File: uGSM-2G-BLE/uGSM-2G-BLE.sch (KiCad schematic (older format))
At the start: 0 parts

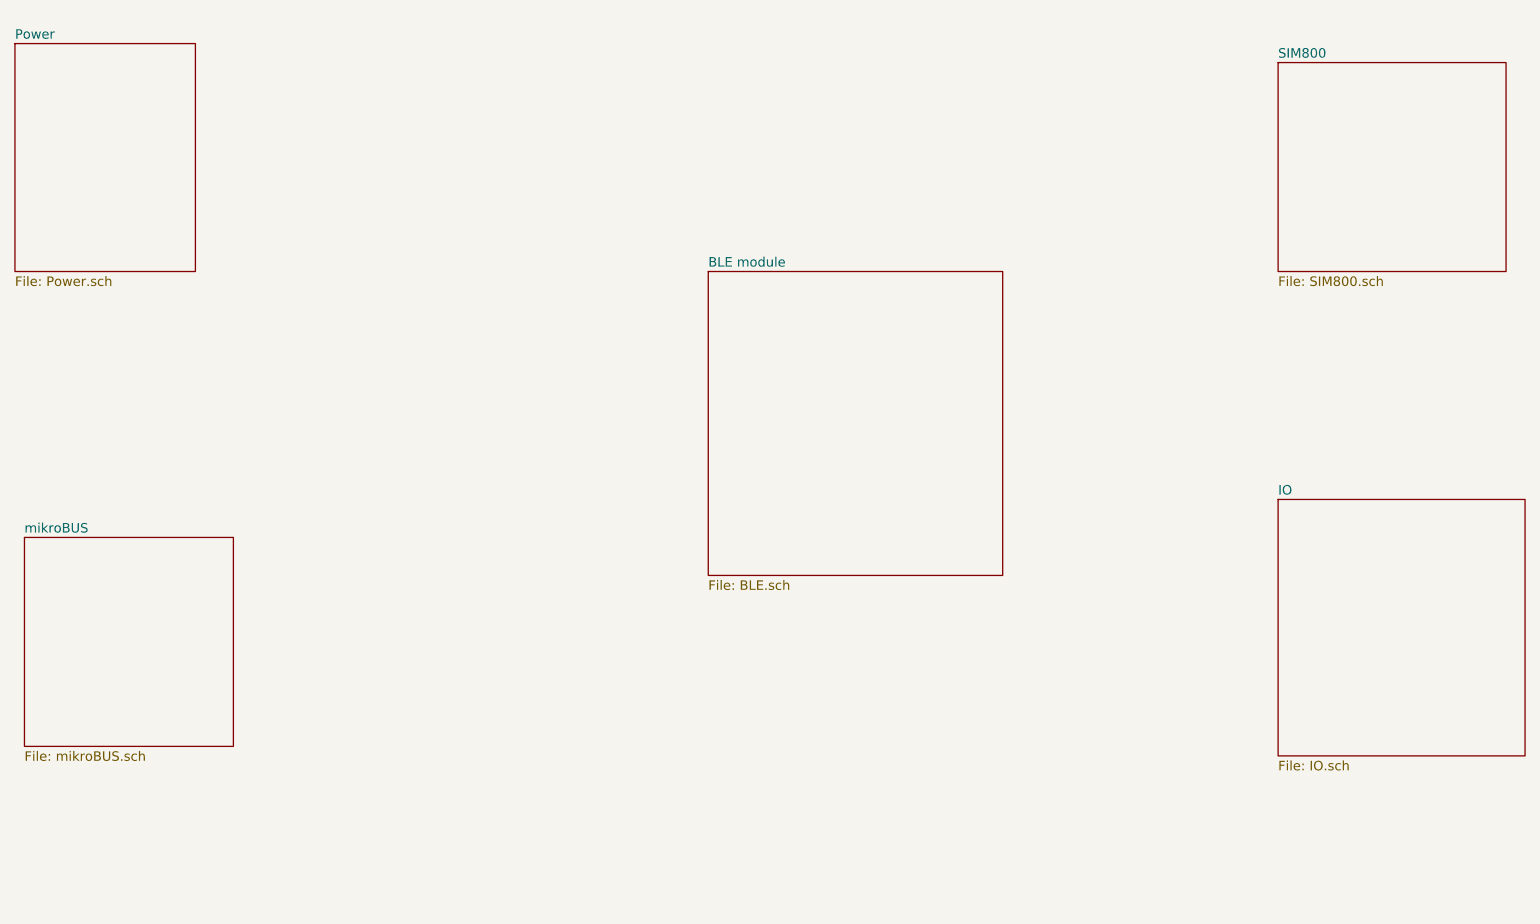
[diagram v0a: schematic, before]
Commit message: added sim800c stuff - needs checking
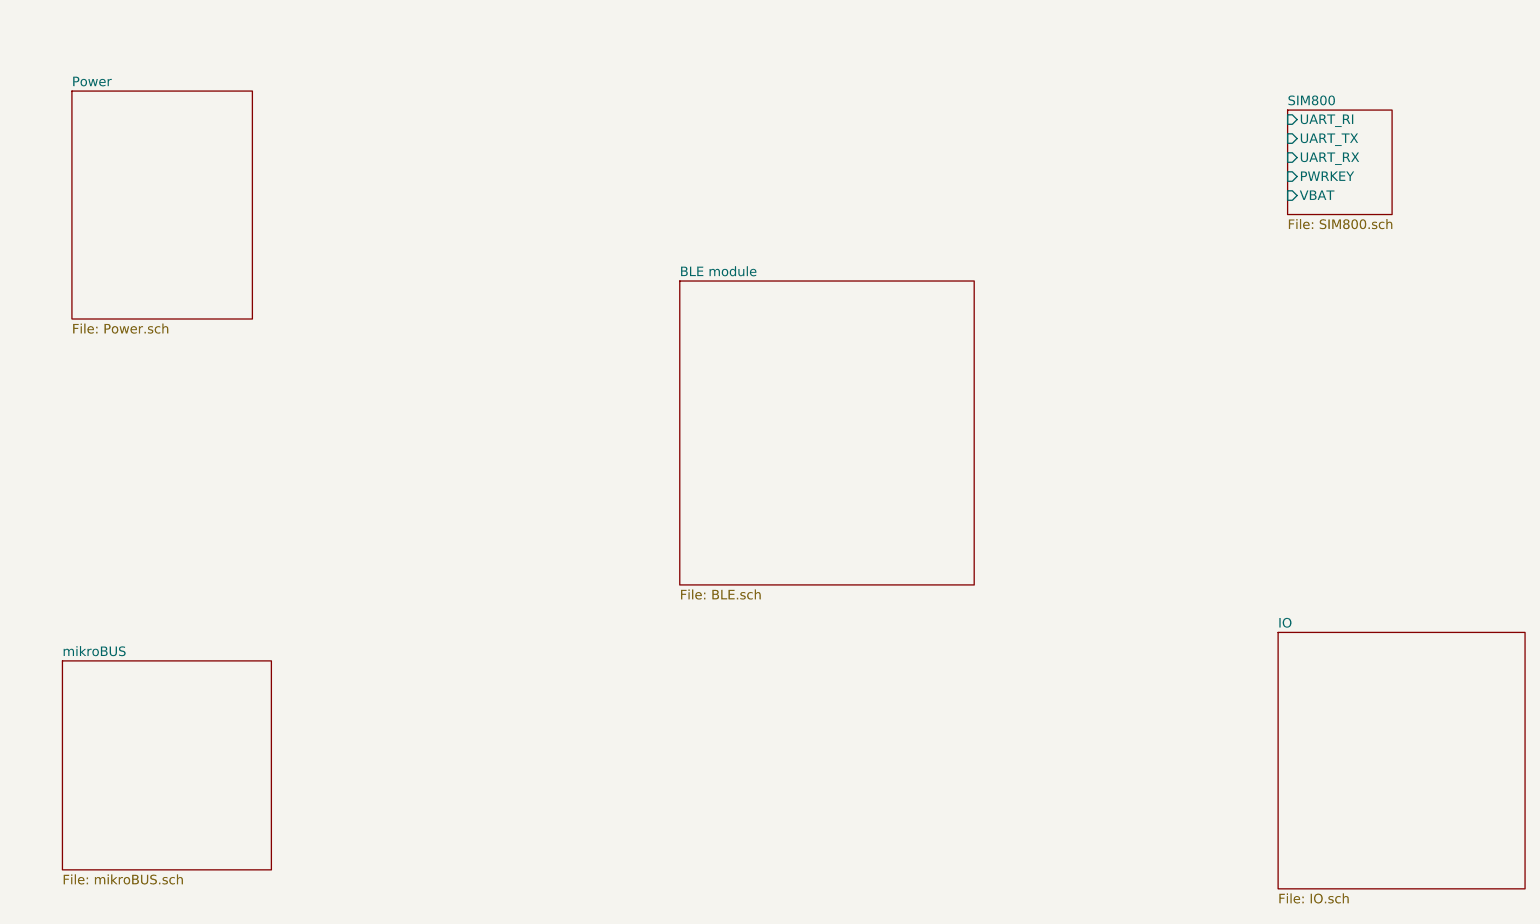
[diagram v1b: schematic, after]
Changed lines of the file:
@@
 $EndDescr
 $Sheet
-S 5350 2950 1550 1600
+S 5200 3000 1550 1600
 U 5E3D7DDA
 F0 "BLE module" 50
@@
 $EndSheet
 $Sheet
-S 1700 1750 950  1200
+S 2000 2000 950  1200
 U 5E3D7E07
 F0 "Power" 50
@@
 $EndSheet
 $Sheet
-S 1750 4350 1100 1100
+S 1950 5000 1100 1100
 U 5E3D7E1D
 F0 "mikroBUS" 50
@@
 $EndSheet
 $Sheet
-S 8350 1850 1200 1100
+S 8400 2100 550  550
 U 5E3D7E36
 F0 "SIM800" 50
 F1 "SIM800.sch" 50
+F2 "UART_TX" I L 8400 2250 50
+F3 "UART_RX" I L 8400 2350 50
+F4 "PWRKEY" I L 8400 2450 50
+F5 "VBAT" I L 8400 2550 50
+F6 "UART_RI" I L 8400 2150 50
 $EndSheet
 $Sheet
-S 8350 4150 1300 1350
+S 8350 4850 1300 1350
 U 5E3D7E53
 F0 "IO" 50

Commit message: ble connected to mikrobus
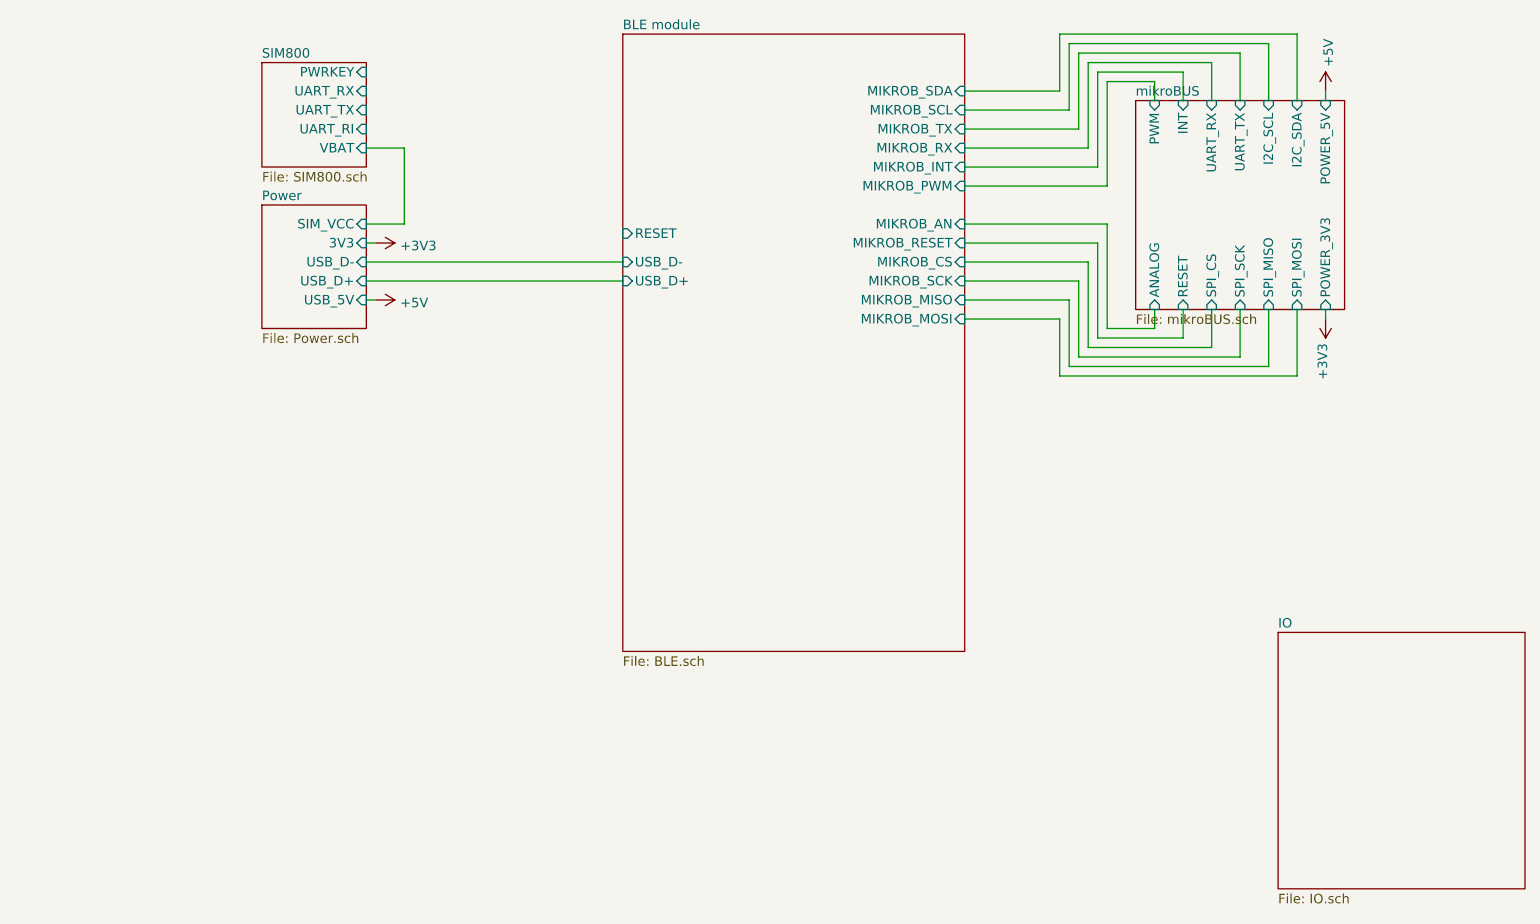
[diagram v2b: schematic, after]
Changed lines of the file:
@@
 $EndDescr
 $Sheet
-S 5200 3000 1550 1600
-U 5E3D7DDA
-F0 "BLE module" 50
-F1 "BLE.sch" 50
-$EndSheet
-$Sheet
-S 2000 2000 950  1200
+S 3000 2600 550  650
 U 5E3D7E07
 F0 "Power" 50
 F1 "Power.sch" 50
-$EndSheet
-$Sheet
-S 1950 5000 1100 1100
+F2 "SIM_VCC" I R 3550 2700 50
+F3 "3V3" I R 3550 2800 50
+F4 "USB_D-" I R 3550 2900 50
+F5 "USB_D+" I R 3550 3000 50
+F6 "USB_5V" I R 3550 3100 50
+$EndSheet
+$Sheet
+S 7600 2050 1100 1100
 U 5E3D7E1D
 F0 "mikroBUS" 50
 F1 "mikroBUS.sch" 50
-$EndSheet
-$Sheet
-S 8400 2100 550  550
+F2 "ANALOG" I B 7700 3150 50
+F3 "RESET" I B 7850 3150 50
+F4 "SPI_CS" I B 8000 3150 50
+F5 "SPI_SCK" I B 8150 3150 50
+F6 "SPI_MISO" I B 8300 3150 50
+F7 "SPI_MOSI" I B 8450 3150 50
+F8 "POWER_3V3" I B 8600 3150 50
+F9 "POWER_5V" I T 8600 2050 50
+F10 "I2C_SDA" I T 8450 2050 50
+F11 "I2C_SCL" I T 8300 2050 50
+F12 "UART_TX" I T 8150 2050 50
+F13 "UART_RX" I T 8000 2050 50
+F14 "INT" I T 7850 2050 50
+F15 "PWM" I T 7700 2050 50
+$EndSheet
+$Sheet
+S 3000 1850 550  550
 U 5E3D7E36
 F0 "SIM800" 50
 F1 "SIM800.sch" 50
-F2 "UART_TX" I L 8400 2250 50
-F3 "UART_RX" I L 8400 2350 50
-F4 "PWRKEY" I L 8400 2450 50
-F5 "VBAT" I L 8400 2550 50
-F6 "UART_RI" I L 8400 2150 50
+F2 "UART_TX" I R 3550 2100 50
+F3 "UART_RX" I R 3550 2000 50
+F4 "PWRKEY" I R 3550 1900 50
+F5 "VBAT" I R 3550 2300 50
+F6 "UART_RI" I R 3550 2200 50
 $EndSheet
 $Sheet
@@
 F1 "IO.sch" 50
 $EndSheet
+$Comp
+L power:+3V3 #PWR?
+U 1 1 5E4C2654
+P 3600 2800
+F 0 "#PWR?" H 3600 2650 50  0001 C CNN
+F 1 "+3V3" V 3615 2928 50  0000 L CNN
+F 2 "" H 3600 2800 50  0001 C CNN
+F 3 "" H 3600 2800 50  0001 C CNN
+	1    3600 2800
+	0    1    1    0
+$EndComp
+$Comp
+L power:+5V #PWR?
+U 1 1 5E4C2986
+P 3600 3100
+F 0 "#PWR?" H 3600 2950 50  0001 C CNN
+F 1 "+5V" V 3615 3228 50  0000 L CNN
+F 2 "" H 3600 3100 50  0001 C CNN
+F 3 "" H 3600 3100 50  0001 C CNN
+	1    3600 3100
+	0    1    1    0
+$EndComp
+Wire Wire Line
+	3550 2800 3600 2800
+Wire Wire Line
+	3550 3100 3600 3100
+$Comp
+L power:+3V3 #PWR?
+U 1 1 5E4C2E8B
+P 8600 3200
+F 0 "#PWR?" H 8600 3050 50  0001 C CNN
+F 1 "+3V3" V 8615 3328 50  0000 L CNN
+F 2 "" H 8600 3200 50  0001 C CNN
+F 3 "" H 8600 3200 50  0001 C CNN
+	1    8600 3200
+	-1   0    0    1
+$EndComp
+$Comp
+L power:+5V #PWR?
+U 1 1 5E4C3500
+P 8600 2000
+F 0 "#PWR?" H 8600 1850 50  0001 C CNN
+F 1 "+5V" V 8615 2128 50  0000 L CNN
+F 2 "" H 8600 2000 50  0001 C CNN
+F 3 "" H 8600 2000 50  0001 C CNN
+	1    8600 2000
+	1    0    0    -1
+$EndComp
+Wire Wire Line
+	8600 2000 8600 2050
+Wire Wire Line
+	8600 3200 8600 3150
+Wire Wire Line
+	3550 2700 3750 2700
+Wire Wire Line
+	3750 2700 3750 2300
+Wire Wire Line
+	3750 2300 3550 2300
+Wire Wire Line
+	3550 2900 4900 2900
+Wire Wire Line
+	3550 3000 4900 3000
+$Sheet
+S 4900 1700 1800 3250
+U 5E3D7DDA
+F0 "BLE module" 50
+F1 "BLE.sch" 50
+F2 "USB_D-" I L 4900 2900 50
+F3 "USB_D+" I L 4900 3000 50
+F4 "RESET" I L 4900 2750 50
+F5 "MIKROB_AN" I R 6700 2700 50
+F6 "MIKROB_RESET" I R 6700 2800 50
+F7 "MIKROB_PWM" I R 6700 2500 50
+F8 "MIKROB_INT" I R 6700 2400 50
+F9 "MIKROB_CS" I R 6700 2900 50
+F10 "MIKROB_TX" I R 6700 2200 50
+F11 "MIKROB_RX" I R 6700 2300 50
+F12 "MIKROB_SCL" I R 6700 2100 50
+F13 "MIKROB_SDA" I R 6700 2000 50
+F14 "MIKROB_SCK" I R 6700 3000 50
+F15 "MIKROB_MOSI" I R 6700 3200 50
+F16 "MIKROB_MISO" I R 6700 3100 50
+$EndSheet
+Wire Wire Line
+	6700 2700 7450 2700
+Wire Wire Line
+	7450 2700 7450 3250
+Wire Wire Line
+	7450 3250 7700 3250
+Wire Wire Line
+	7700 3250 7700 3150
+Wire Wire Line
+	6700 2800 7400 2800
+Wire Wire Line
+	7400 2800 7400 3300
+Wire Wire Line
+	7400 3300 7850 3300
+Wire Wire Line
+	7850 3300 7850 3150
+Wire Wire Line
+	6700 2900 7350 2900
+Wire Wire Line
+	7350 2900 7350 3350
+Wire Wire Line
+	7350 3350 8000 3350
+Wire Wire Line
+	8000 3350 8000 3150
+Wire Wire Line
+	6700 3000 7300 3000
+Wire Wire Line
+	7300 3000 7300 3400
+Wire Wire Line
+	7300 3400 8150 3400
+Wire Wire Line
+	8150 3400 8150 3150
+Wire Wire Line
+	6700 3100 7250 3100
+Wire Wire Line
+	7250 3100 7250 3450
+Wire Wire Line
+	7250 3450 8300 3450
+Wire Wire Line
+	8300 3450 8300 3150
+Wire Wire Line
+	6700 3200 7200 3200
+Wire Wire Line
+	7200 3200 7200 3500
+Wire Wire Line
+	7200 3500 8450 3500
+Wire Wire Line
+	8450 3500 8450 3150
+Wire Wire Line
+	6700 2500 7450 2500
+Wire Wire Line
+	7450 2500 7450 1950
+Wire Wire Line
+	7450 1950 7700 1950
+Wire Wire Line
+	7700 1950 7700 2050
+Wire Wire Line
+	6700 2400 7400 2400
+Wire Wire Line
+	7400 2400 7400 1900
+Wire Wire Line
+	7400 1900 7850 1900
+Wire Wire Line
+	7850 1900 7850 2050
+Wire Wire Line
+	6700 2300 7350 2300
+Wire Wire Line
+	7350 2300 7350 1850
+Wire Wire Line
+	7350 1850 8000 1850
+Wire Wire Line
+	8000 1850 8000 2050
+Wire Wire Line
+	6700 2200 7300 2200
+Wire Wire Line
+	7300 2200 7300 1800
+Wire Wire Line
+	7300 1800 8150 1800
+Wire Wire Line
+	8150 1800 8150 2050
+Wire Wire Line
+	6700 2100 7250 2100
+Wire Wire Line
+	7250 2100 7250 1750
+Wire Wire Line
+	7250 1750 8300 1750
+Wire Wire Line
+	8300 1750 8300 2050
+Wire Wire Line
+	6700 2000 7200 2000
+Wire Wire Line
+	7200 2000 7200 1700
+Wire Wire Line
+	7200 1700 8450 1700
+Wire Wire Line
+	8450 1700 8450 2050
 $EndSCHEMATC

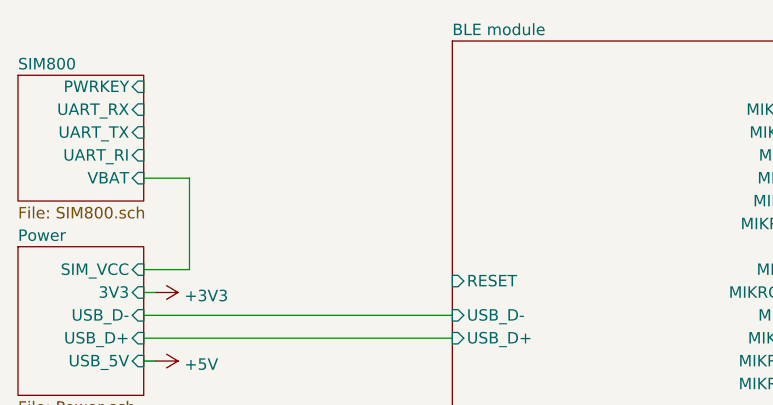
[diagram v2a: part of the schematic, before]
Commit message: removed usbl6 simcom
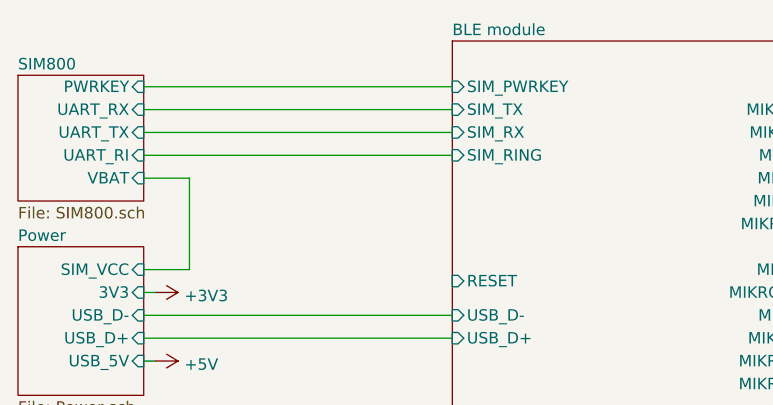
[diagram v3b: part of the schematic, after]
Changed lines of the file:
@@
 F15 "MIKROB_MOSI" I R 6700 3200 50
 F16 "MIKROB_MISO" I R 6700 3100 50
+F17 "SIM_RX" I L 4900 2100 50
+F18 "SIM_TX" I L 4900 2000 50
+F19 "SIM_PWRKEY" I L 4900 1900 50
+F20 "SIM_RING" I L 4900 2200 50
 $EndSheet
 Wire Wire Line
@@
 Wire Wire Line
 	8450 1700 8450 2050
+Wire Wire Line
+	3550 1900 4900 1900
+Wire Wire Line
+	3550 2000 4900 2000
+Wire Wire Line
+	3550 2100 4900 2100
+Wire Wire Line
+	3550 2200 4900 2200
 $EndSCHEMATC
